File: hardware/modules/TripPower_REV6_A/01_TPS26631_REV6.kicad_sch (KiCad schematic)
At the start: 13 parts, among them Q201 SQM100N10-10_GE3 100V AEC, Q202 BSS138LT1G DRIVER PULLDOWN, U201 TPS26631PWPR

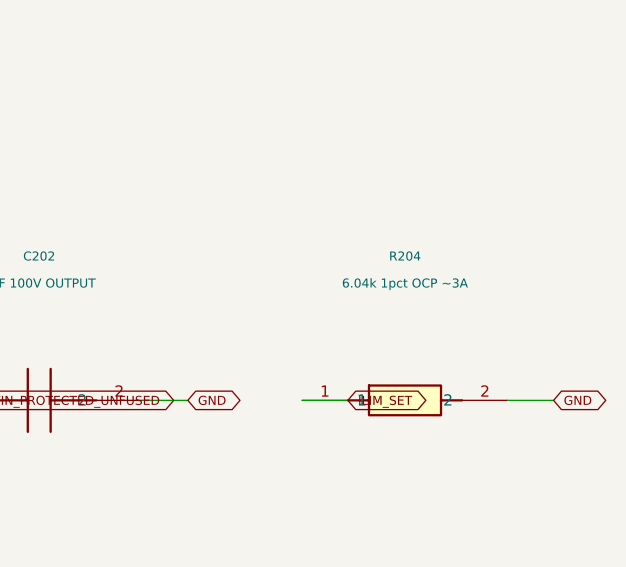
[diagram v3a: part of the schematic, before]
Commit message: REV6 A: replace out-of-stock 6k04 ILIM resistor with stocked Vishay AEC-Q200 CRCW12066K04FKEAHP
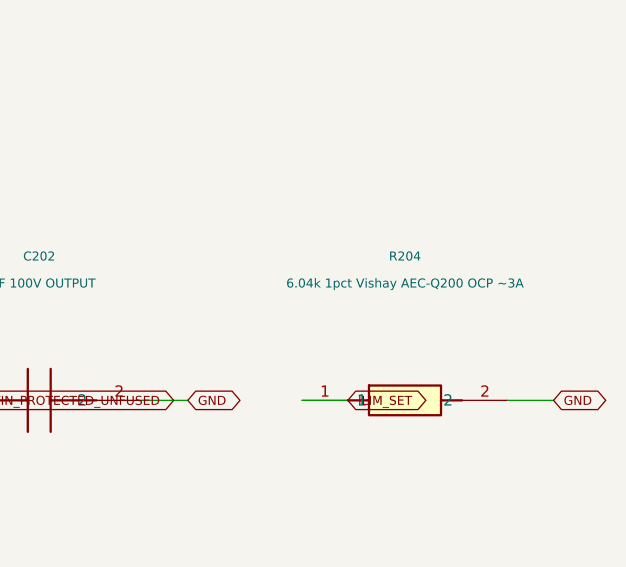
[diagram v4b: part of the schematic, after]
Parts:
- R204: value 6.04k 1pct OCP ~3A -> 6.04k 1pct Vishay AEC-Q200 OCP ~3A; MPN AC1206FR-076K04L -> CRCW12066K04FKEAHP
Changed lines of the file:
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@@
 (symbol (lib_id "Tripmaster_Sym:R") (at 396.24 205.74 0) (unit 1) (in_bom yes) (on_board yes) (dnp no)
 (property "Reference" "R204" (at 396.24 189.74 0) (effects (font (size 1 1))))
-(property "Value" "6.04k 1pct OCP ~3A" (at 396.24 192.74 0) (effects (font (size 1 1))))
+(property "Value" "6.04k 1pct Vishay AEC-Q200 OCP ~3A" (at 396.24 192.74 0) (effects (font (size 1 1))))
 (property "Footprint" "Resistor_SMD:R_1206_3216Metric" (at 396.24 205.74 0) (effects (font (size 1 1)) (hide yes)))
-(property "MPN" "AC1206FR-076K04L" (at 0 0 0) (effects (font (size 1 1)) (hide yes)))
+(property "MPN" "CRCW12066K04FKEAHP" (at 0 0 0) (effects (font (size 1 1)) (hide yes)))
 (pin "1")
 (pin "2")
